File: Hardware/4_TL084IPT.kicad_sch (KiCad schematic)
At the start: 23 parts, among them J10 Screw_Terminal_01x08, Q12 N_Mosfet, Q13 N_Mosfet, Q14 N_Mosfet, Q15 N_Mosfet, U14 TL084

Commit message: layout part 2
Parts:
- D20, D21, D22, D23: footprint IVS_FOOTPRINTS:D_MiniMELF -> IVS_FOOTPRINTS:D_SOD323
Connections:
- net VAN13_output: now also R92.2, U14.7; no longer R91.2, U14.1
- net VAN14_output: now also R91.2, U14.1; no longer R92.2, U14.7
- net VAN15_output: now also R94.2, U14.14; no longer R93.2, U14.8
- net VAN16_output: now also R93.2, U14.8; no longer R94.2, U14.14
- net at Q13.2 (S), R84.1: now also U14.3 (+); no longer U14.5 (+)
- net at Q14.2 (S), R85.1: now also U14.12 (+); no longer U14.10 (+)
- net at Q12.2 (S), R83.1: now also U14.5 (+); no longer U14.3 (+)
- net at Q15.2 (S), R86.1: now also U14.10 (+); no longer U14.12 (+)
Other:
- moved on the sheet: C31, R91, R92, R93, R94, U14A, U14B, U14C, U14D, U14E

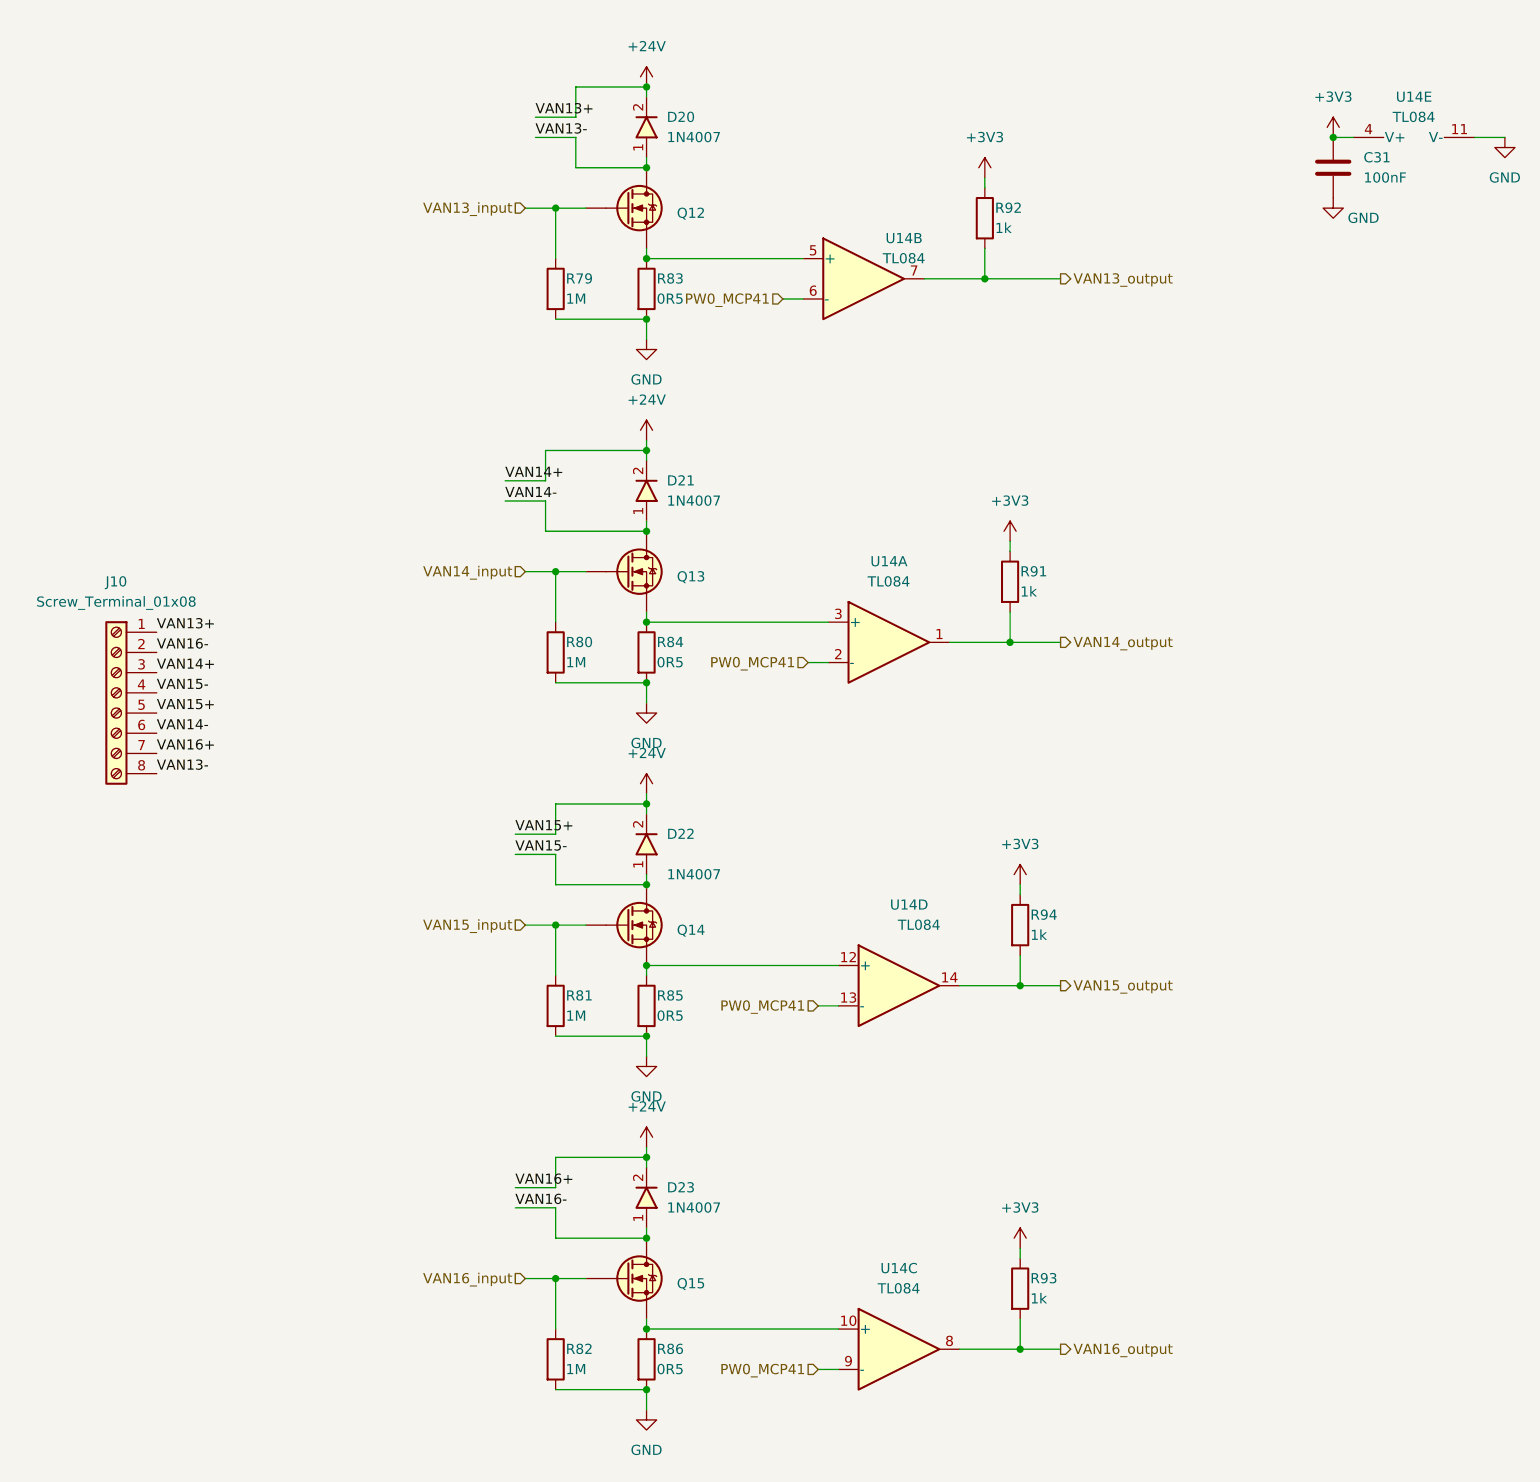
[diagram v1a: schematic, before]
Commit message: add lora, relay, opto, opamp block, led for 74595. Delete RT9193, connect boot0,1 to GND. Fix footprint crystal 8M, 74HC595, IDC pin
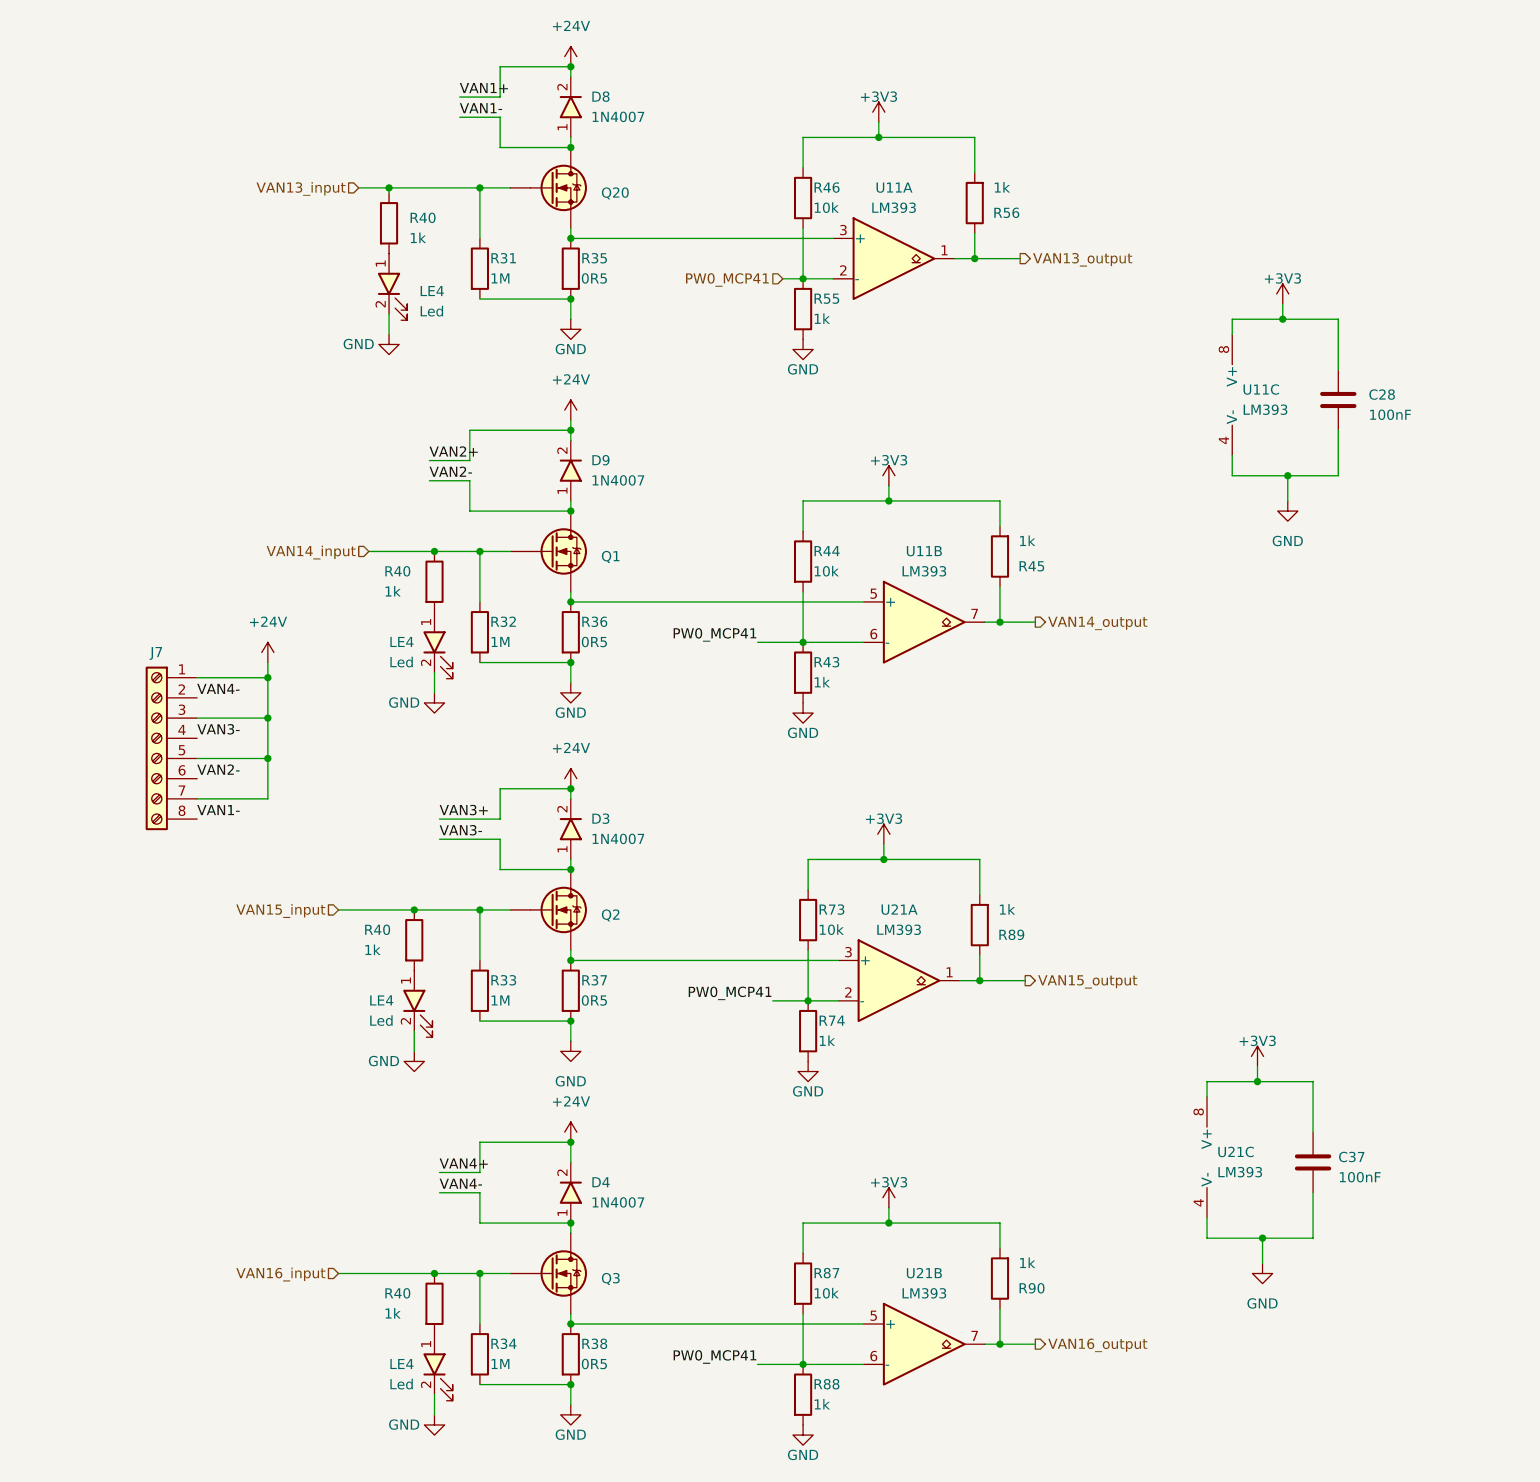
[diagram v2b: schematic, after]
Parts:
- removed C31: 100nF, IVS_FOOTPRINTS:C0603, symbol Device:C
- removed D20, D21, D22, D23: 1N4007, IVS_FOOTPRINTS:D_SOD323, symbol IVS_SYMBOL_DIR:D_Diode
- removed J10: Screw_Terminal_01x08, IVS_FOOTPRINTS:HT-3.96mm, symbol Connector:Screw_Terminal_01x08
- removed Q12, Q13, Q14, Q15: N_Mosfet, IVS_FOOTPRINTS:SOT23-3, symbol IVS_SYMBOLS:N_Mosfet
- removed R79, R80, R81, R82: 1M, IVS_FOOTPRINTS:R0603, symbol Device:R
- removed R83, R84, R85, R86: 0R5, Resistor_SMD:R_0805_2012Metric, symbol Device:R
- removed R91, R92, R93, R94: 1k, IVS_FOOTPRINTS:R0603, symbol Device:R
- removed U14: TL084, IVS_FOOTPRINTS:TSSOP14, symbol Amplifier_Operational:TL084
- added C28, C37: 100nF, IVS_FOOTPRINTS:C_0603, symbol Device:C
- added D3, D4, D8, D9: 1N4007, IVS_FOOTPRINTS:D_SOD323, symbol IVS_SYMBOL_DIR:D_Diode
- added J7: Screw_Terminal_01x08, IVS_FOOTPRINTS:HT-3.96mm, symbol Connector:Screw_Terminal_01x08
- added LE4 (x4): Led, IVS_FOOTPRINTS:LED_0603, symbol IVS_SYMBOLS:Led
- added Q1, Q2, Q20, Q3: N_Mosfet, IVS_FOOTPRINTS:SOT23-3, symbol IVS_SYMBOLS:N_Mosfet
- added R31, R32, R33, R34: 1M, IVS_FOOTPRINTS:R_0603, symbol Device:R
- added R35, R36, R37, R38: 0R5, IVS_FOOTPRINTS:R_0805, symbol Device:R
- added R40 (x4), R43, R45, R55, R56, R74, R88, R89, R90: 1k, IVS_FOOTPRINTS:R_0603, symbol Device:R
- added R44, R46, R73, R87: 10k, IVS_FOOTPRINTS:R_0603, symbol Device:R
- added U11, U21: LM393, IVS_FOOTPRINTS:SOIC-8_3.9x4.9mm_P1.27mm, symbol Comparator:LM393
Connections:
- net +24V: now also D3.2, D4.2, D8.2, D9.2, J7.1 (Pin_1), J7.3 (Pin_3), J7.5 (Pin_5), J7.7 (Pin_7)
- net +3V3: now also C28.1, C37.1, R44.1, R45.2, R46.1, R56.2, R73.1, R87.1, R89.2, R90.2, U11.8 (V+), U21.8 (V+)
- net GND: now also C28.2, C37.2, LE4.2, LE4.2, LE4.2, LE4.2, R31.2, R32.2, R33.2, R34.2, R35.2, R36.2, R37.2, R38.2, R43.2, R55.2, R74.2, R88.2, U11.4 (V-), U21.4 (V-)
- net PW0_MCP41: now also R43.1, R44.2, R46.2, R55.1, R73.2, R74.1, R87.2, R88.1, U11.2 (-), U11.6 (-), U21.2 (-), U21.6 (-)
- net VAN13_input: now also Q20.1 (G), R31.1, R40.1
- net VAN13_output: now also R56.1, U11.1
- net VAN14_input: now also Q1.1 (G), R32.1, R40.1
- net VAN14_output: now also R45.1, U11.7
- net VAN15_input: now also Q2.1 (G), R33.1, R40.1
- net VAN15_output: now also R89.1, U21.1
- net VAN16_input: now also Q3.1 (G), R34.1, R40.1
- net VAN16_output: now also R90.1, U21.7
- new net: Q2.2 (S), R37.1, U21.3 (+)
- new net: Q20.2 (S), R35.1, U11.3 (+)
- new net: LE4.1, R40.2 (x4)
- new net: Q1.2 (S), R36.1, U11.5 (+)
- new net: Q3.2 (S), R38.1, U21.5 (+)
- new net VAN1-: D8.1, J7.8 (Pin_8), Q20.3 (D)
- new net VAN2-: D9.1, J7.6 (Pin_6), Q1.3 (D)
- new net VAN3-: D3.1, J7.4 (Pin_4), Q2.3 (D)
- new net VAN4-: D4.1, J7.2 (Pin_2), Q3.3 (D)
